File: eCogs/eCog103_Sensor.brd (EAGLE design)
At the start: 47.5 x 28 mm, 7 parts

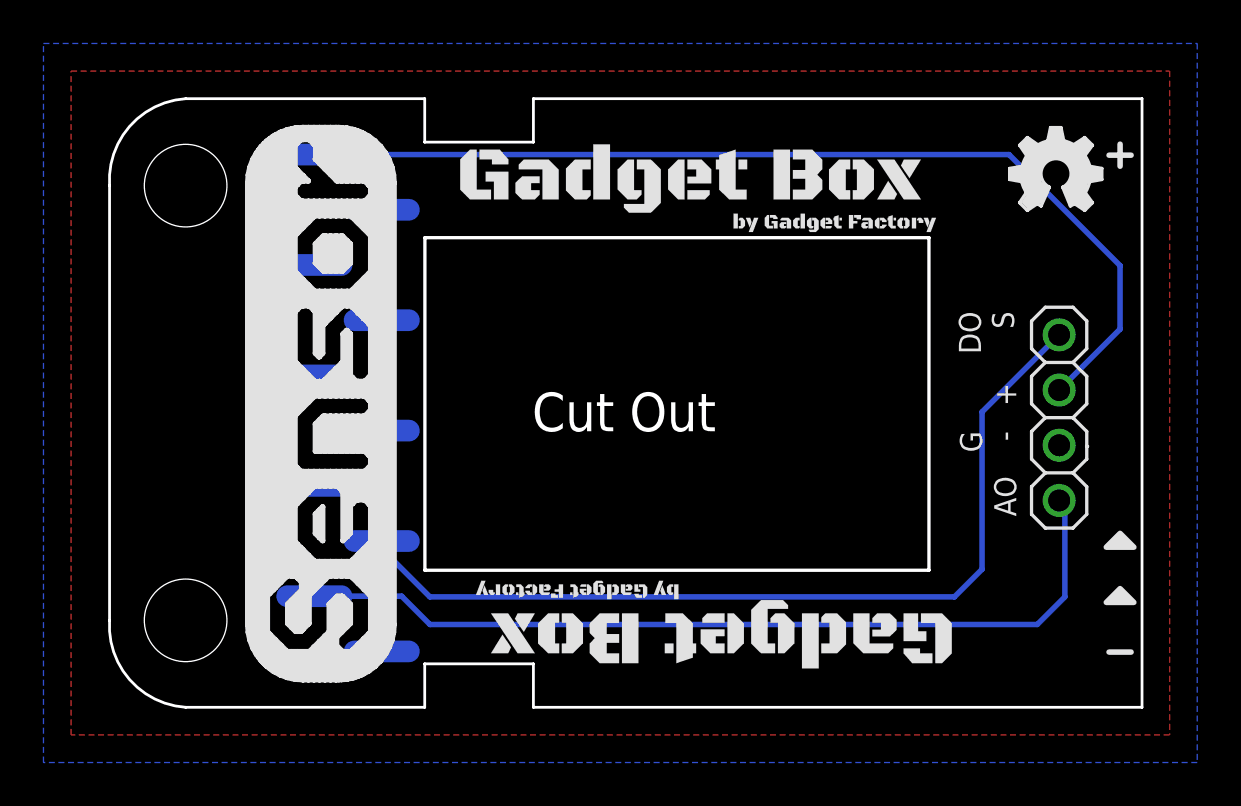
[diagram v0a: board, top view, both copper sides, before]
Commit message: Flipped the sensor around to fit in boxes with modules in the middle.
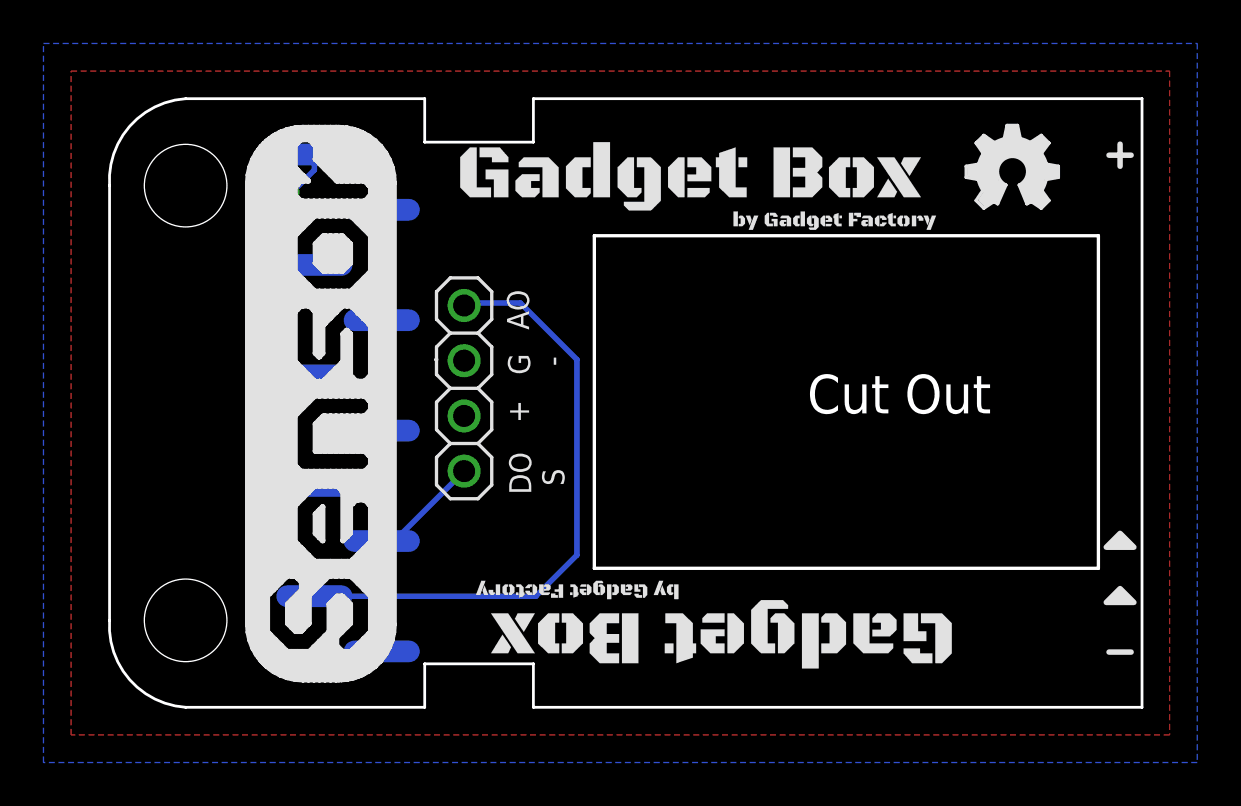
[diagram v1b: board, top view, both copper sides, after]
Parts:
- ECOG: value ECOG_GENERAL_ROWECOG_GENERAL_SMD -> ECOG_GENERAL_ROWSURFACEMOUNT
- moved U$1 31.4 mm to (14.8, 14.7), turned to 90 degrees
- moved U$5 2.00 mm to (39.9, 23.0)
- moved U$4 0.10 mm to (27.3, 24.4)
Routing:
- net 3V3: track 46.1 -> 2.49 mm, vias 0 -> 1
- net A2: track 41.7 -> 5.12 mm
- net A1: track 40.1 -> 28.2 mm
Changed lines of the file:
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@@
 <setting verticaltext="up"/>
 </settings>
-<grid distance="0.05" unitdist="inch" unit="inch" style="lines" multiple="1" display="yes" altdistance="0.005" altunitdist="inch" altunit="inch"/>
+<grid distance="1" unitdist="mm" unit="mm" style="lines" multiple="1" display="yes" altdistance="0.1" altunitdist="mm" altunit="mm"/>
 <layers>
 <layer number="1" name="Top" color="4" fill="1" visible="yes" active="yes"/>
@@
 <layer number="19" name="Unrouted" color="6" fill="1" visible="yes" active="yes"/>
 <layer number="20" name="Dimension" color="15" fill="1" visible="yes" active="yes"/>
-<layer number="21" name="tPlace" color="16" fill="1" visible="no" active="yes"/>
+<layer number="21" name="tPlace" color="16" fill="1" visible="yes" active="yes"/>
 <layer number="22" name="bPlace" color="14" fill="1" visible="yes" active="yes"/>
 <layer number="23" name="tOrigins" color="15" fill="1" visible="yes" active="yes"/>
@@
 <text x="16.161" y="24.765" size="1.016" layer="22" font="vector" rot="MR0">3.3V</text>
 <text x="9.43" y="2.286" size="1.016" layer="22" font="vector" rot="MR0">GND</text>
-<text x="19.939" y="12.7" size="1.778" layer="20" font="vector" ratio="15">Cut Out</text>
+<text x="41.061" y="15.3" size="1.778" layer="20" font="vector" ratio="15" rot="R180">Cut Out</text>
 <wire x1="9.971" y1="8.0023" x2="9.971" y2="8.8855" width="0.254" layer="21"/>
 <wire x1="9.971" y1="8.8855" x2="10.16" y2="9.0745" width="0.254" layer="21"/>
@@
 </autorouter>
 <elements>
-<element name="ECOG" library="eCogs" package="ECOG_GENERAL_SMD" value="ECOG_GENERAL_ROWECOG_GENERAL_SMD" x="0" y="0" smashed="yes">
+<element name="ECOG" library="eCogs" package="ECOG_GENERAL_SMD" value="ECOG_GENERAL_ROWSURFACEMOUNT" x="0" y="0" smashed="yes">
 <attribute name="DIGIKEY" value="S1013EC-10-ND" x="0" y="0" size="1.778" layer="27" display="off"/>
 </element>
-<element name="U$1" library="eCogs" package="SENSOR-HJX4" value="SENSOR" x="46.197" y="13.305" smashed="yes" rot="R270"/>
+<element name="U$1" library="eCogs" package="SENSOR-HJX4" value="SENSOR" x="14.803" y="14.695" smashed="yes" rot="R90"/>
 <element name="U$2" library="eCogs" package="LEGEND_ANALOG" value="" x="46.99" y="7.62"/>
 <element name="U$3" library="eCogs" package="LEGEND_ANALOG" value="" x="46.99" y="5.08"/>
-<element name="U$4" library="GadgetFactory" package="GADGETBOX_SMALL" value="" x="27.305" y="24.257"/>
-<element name="U$5" library="ohw-logo" package="OSHW_FILLX150_NOTEXT" value="" x="41.91" y="22.86"/>
+<element name="U$4" library="GadgetFactory" package="GADGETBOX_SMALL" value="" x="27.305" y="24.357"/>
+<element name="U$5" library="ohw-logo" package="OSHW_FILLX150_NOTEXT" value="" x="39.91" y="22.96"/>
 <element name="U$6" library="GadgetFactory" package="GADGETBOX_SMALL" value="" x="28.575" y="3.429" rot="R180"/>
 </elements>
@@
 <contactref element="U$1" pad="+"/>
 <contactref element="ECOG" pad="3V3"/>
-<wire x1="9.92324375" y1="25.429" x2="41.881" y2="25.429" width="0.254" layer="16"/>
-<wire x1="41.881" y1="25.429" x2="46.99" y2="20.32" width="0.254" layer="16"/>
-<wire x1="46.99" y1="20.32" x2="46.99" y2="17.398" width="0.254" layer="16"/>
-<wire x1="46.99" y1="17.398" x2="44.187" y2="14.595" width="0.254" layer="16"/>
+<wire x1="9.92324375" y1="25.429" x2="9.92324375" y2="24.72324375" width="0.254" layer="16"/>
+<wire x1="9.92324375" y1="24.72324375" x2="8.9" y2="23.7" width="0.254" layer="16"/>
+<via x="8.9" y="23.7" extent="1-16" drill="0.381"/>
+<wire x1="8.9" y1="23.7" x2="8.7" y2="23.7" width="0.254" layer="1"/>
+<wire x1="8.7" y1="23.7" x2="8.6" y2="23.6" width="0.254" layer="1"/>
 </signal>
 <signal name="A2">
 <contactref element="U$1" pad="DO/S"/>
 <contactref element="ECOG" pad="G1"/>
-<wire x1="13.02204375" y1="7.649" x2="13.02204375" y2="7.29795625" width="0.254" layer="16"/>
-<wire x1="13.02204375" y1="7.29795625" x2="15.24" y2="5.08" width="0.254" layer="16"/>
-<wire x1="15.24" y1="5.08" x2="39.37" y2="5.08" width="0.254" layer="16"/>
-<wire x1="39.37" y1="5.08" x2="40.64" y2="6.35" width="0.254" layer="16"/>
-<wire x1="40.64" y1="6.35" x2="40.64" y2="13.588" width="0.254" layer="16"/>
-<wire x1="40.64" y1="13.588" x2="44.187" y2="17.135" width="0.254" layer="16"/>
+<wire x1="13.02204375" y1="7.649" x2="13.597" y2="7.649" width="0.254" layer="16"/>
+<wire x1="13.597" y1="7.649" x2="16.813" y2="10.865" width="0.254" layer="16"/>
 </signal>
 <signal name="A1">
 <contactref element="U$1" pad="AO"/>
 <contactref element="ECOG" pad="G0"/>
-<wire x1="9.92324375" y1="5.1110625" x2="13.9389375" y2="5.1110625" width="0.254" layer="16"/>
-<wire x1="13.9389375" y1="5.1110625" x2="15.24" y2="3.81" width="0.254" layer="16"/>
-<wire x1="15.24" y1="3.81" x2="43.18" y2="3.81" width="0.254" layer="16"/>
-<wire x1="43.18" y1="3.81" x2="44.45" y2="5.08" width="0.254" layer="16"/>
-<wire x1="44.45" y1="5.08" x2="44.45" y2="9.252" width="0.254" layer="16"/>
-<wire x1="44.45" y1="9.252" x2="44.187" y2="9.515" width="0.254" layer="16"/>
+<wire x1="9.92324375" y1="5.1110625" x2="20.1110625" y2="5.1110625" width="0.254" layer="16"/>
+<wire x1="20.1110625" y1="5.1110625" x2="22" y2="7" width="0.254" layer="16"/>
+<wire x1="22" y1="7" x2="22" y2="16" width="0.254" layer="16"/>
+<wire x1="22" y1="16" x2="19.4" y2="18.6" width="0.254" layer="16"/>
+<wire x1="19.4" y1="18.6" x2="16.928" y2="18.6" width="0.254" layer="16"/>
+<wire x1="16.928" y1="18.6" x2="16.813" y2="18.485" width="0.254" layer="16"/>
 </signal>
 </signals>
